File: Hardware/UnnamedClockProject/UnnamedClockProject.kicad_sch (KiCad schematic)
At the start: 7 parts, among them K101 DIR, K102 EN

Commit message: Bump upstream libs
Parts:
- added A101: Arduino_UNO_R3, Module:Arduino_UNO_R3, symbol MCU_Module:Arduino_UNO_R3
- added D103: FIX, LED_THT:LED_D5.0mm, symbol Device:LED
- added R103: 1k, symbol Device:R_Small
- added U102: ~, ac1ja:Ultimate GPS Breakout V3 Module, symbol ac1ja:Ultimate_GPS_Breakout_v3
- added U103: ~, ac1ja:DS3231, symbol ac1ja:DS3231_Breakout
- D101: value EN_LED -> EN
- D102: value DIR_LED -> DIR
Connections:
- net +5V: now also A101.5 (+5V), U102.8 (VIN), U103.1 (VIN)
- net GND: now also A101.29 (GND), A101.6 (GND), A101.7 (GND), D103.1 (K), U102.7 (GND), U103.2 (GND)
- new net: D103.2 (A), R103.2
- new net: R103.1, U102.4 (FIX)
- new net SCL: A101.14 (SCL/A5), U103.3 (SCL)
- new net SDA: A101.13 (SDA/A4), U103.4 (SDA)
- no-connect marks 1 -> 10

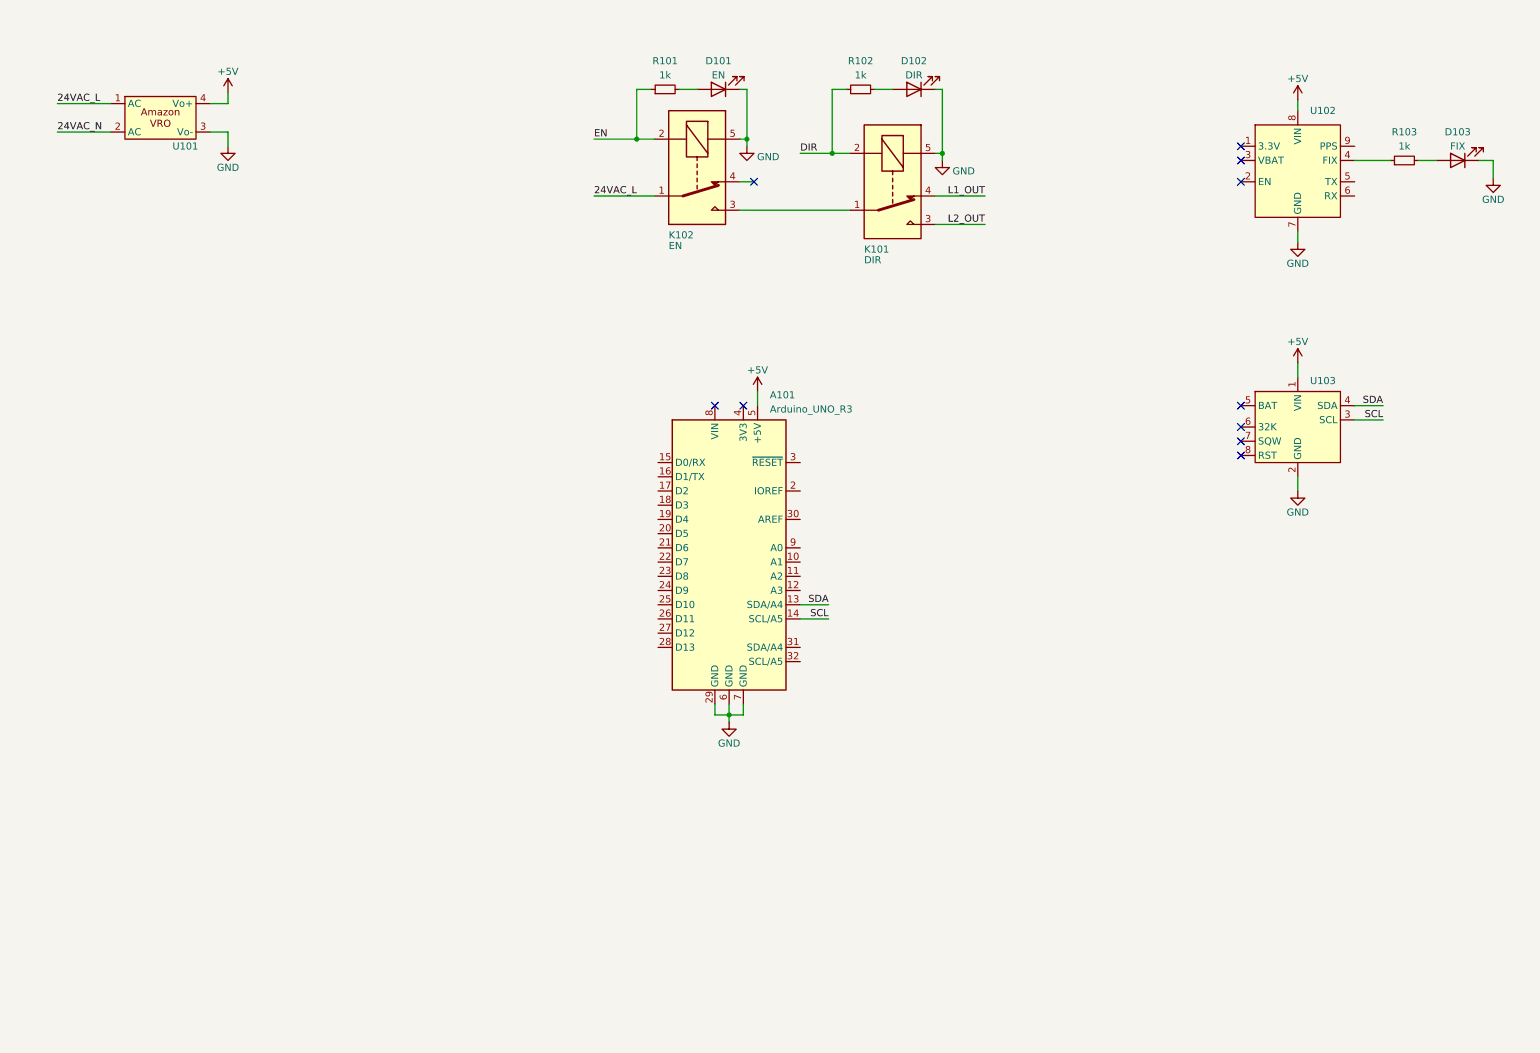
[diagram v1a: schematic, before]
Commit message: Add new design with solid state relays
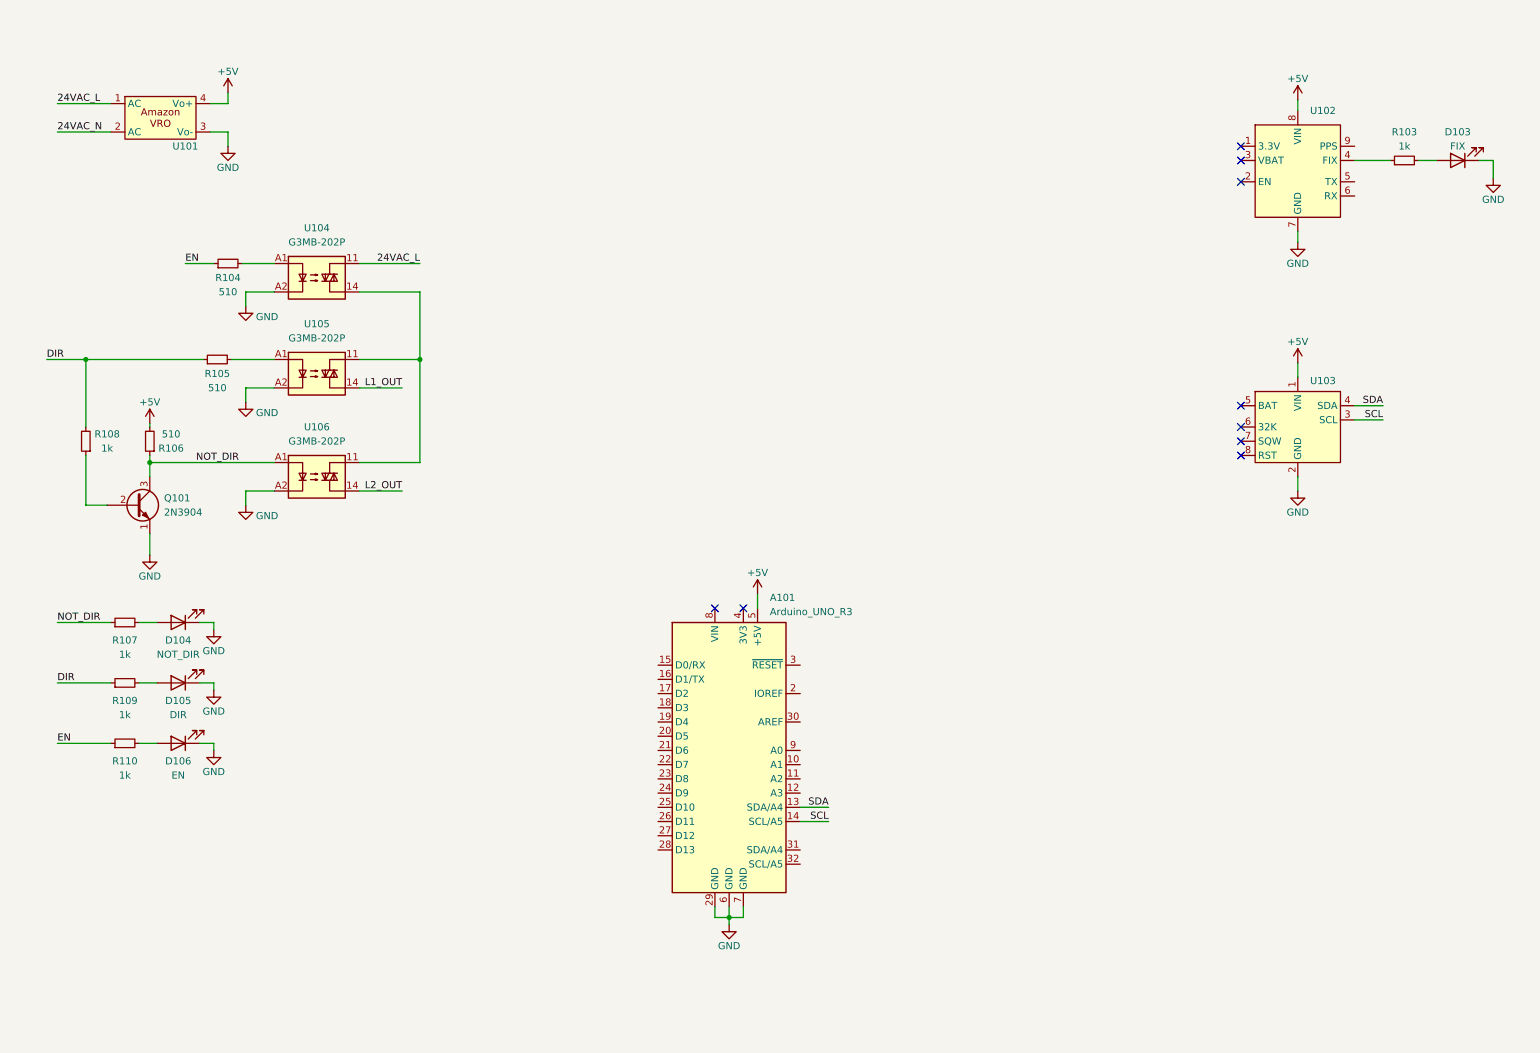
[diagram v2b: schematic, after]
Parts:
- removed D101: EN, LED_THT:LED_D5.0mm, symbol Device:LED
- removed D102: DIR, LED_THT:LED_D5.0mm, symbol Device:LED
- removed K101: DIR, Relay_THT:Relay_SPDT_SANYOU_SRD_Series_Form_C, symbol Relay:SANYOU_SRD_Form_C
- removed K102: EN, Relay_THT:Relay_SPDT_SANYOU_SRD_Series_Form_C, symbol Relay:SANYOU_SRD_Form_C
- removed R101, R102: 1k, symbol Device:R_Small
- added D104: NOT_DIR, LED_THT:LED_D5.0mm, symbol Device:LED
- added D105: DIR, LED_THT:LED_D5.0mm, symbol Device:LED
- added D106: EN, LED_THT:LED_D5.0mm, symbol Device:LED
- added Q101: 2N3904, Package_TO_SOT_THT:TO-92_Inline, symbol Transistor_BJT:2N3904
- added R104, R105, R106: 510, symbol Device:R_Small
- added R107, R108, R109, R110: 1k, symbol Device:R_Small
- added U104, U105, U106: G3MB-202P, symbol Relay_SolidState:34.81-8240
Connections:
- net +5V: now also R106.2
- net 24VAC_L: now also U104.11
- net DIR: now also R105.1, R108.2, R109.1
- net EN: now also R104.1, R110.1
- net GND: now also D104.1 (K), D105.1 (K), D106.1 (K), Q101.1 (E), U104.A2, U105.A2, U106.A2
- net L1_OUT: now also U105.14
- net L2_OUT: now also U106.14
- new net: U104.14, U105.11, U106.11
- new net: R104.2, U104.A1
- new net: D105.2 (A), R109.2
- new net: D106.2 (A), R110.2
- new net: D104.2 (A), R107.2
- new net: Q101.2 (B), R108.1
- new net: R105.2, U105.A1
- new net NOT_DIR: Q101.3 (C), R106.1, R107.1, U106.A1
- no-connect marks 10 -> 9
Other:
- moved on the sheet: A101

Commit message: Add footprints
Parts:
- U104, U105, U106: footprint (none) -> OptoDevice:Finder_34.81
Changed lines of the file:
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@@
       (effects (font (size 1.27 1.27)))
     )
-    (property "Footprint" "" (at 62.865 65.405 0)
+    (property "Footprint" "OptoDevice:Finder_34.81" (at 62.865 65.405 0)
       (effects (font (size 1.27 1.27) italic) (justify left) hide)
     )
@@
       (effects (font (size 1.27 1.27)))
     )
-    (property "Footprint" "" (at 62.865 82.55 0)
+    (property "Footprint" "OptoDevice:Finder_34.81" (at 62.865 82.55 0)
       (effects (font (size 1.27 1.27) italic) (justify left) hide)
     )
@@
       (effects (font (size 1.27 1.27)))
     )
-    (property "Footprint" "" (at 62.865 100.965 0)
+    (property "Footprint" "OptoDevice:Finder_34.81" (at 62.865 100.965 0)
       (effects (font (size 1.27 1.27) italic) (justify left) hide)
     )

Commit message: Add plugs
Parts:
- added J101: CLOCK_OUT, TerminalBlock_WAGO:TerminalBlock_WAGO_236-103_1x03_P5.00mm_45Degree, symbol Connector:Screw_Terminal_01x03
- added J102: POWER, TerminalBlock_WAGO:TerminalBlock_WAGO_236-103_1x03_P5.00mm_45Degree, symbol Connector:Screw_Terminal_01x03
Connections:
- net 24VAC_L: now also J102.1 (Pin_1)
- net 24VAC_N: now also J101.1 (Pin_1), J102.3 (Pin_3)
- net GND: now also J102.2 (Pin_2)
- net L1_OUT: now also J101.2 (Pin_2)
- net L2_OUT: now also J101.3 (Pin_3)
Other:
- moved on the sheet: D104, D105, D106, Q101, R104, R105, R106, R107, R108, R109, R110, U104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

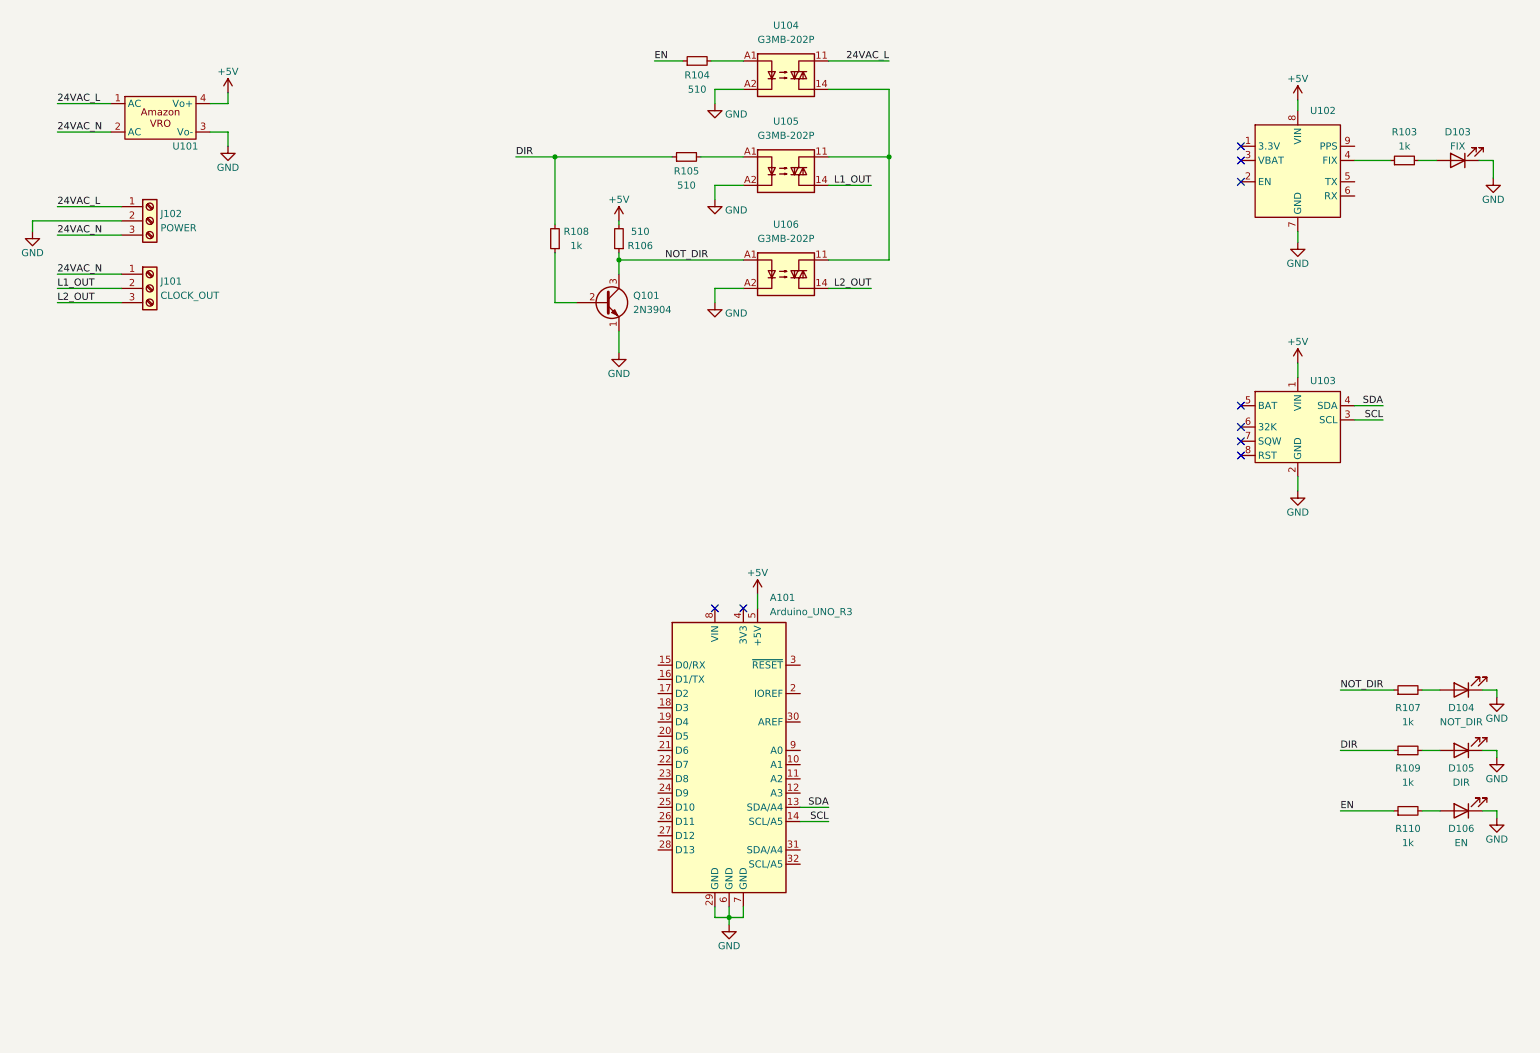
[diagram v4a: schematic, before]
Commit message: Tie into mcu
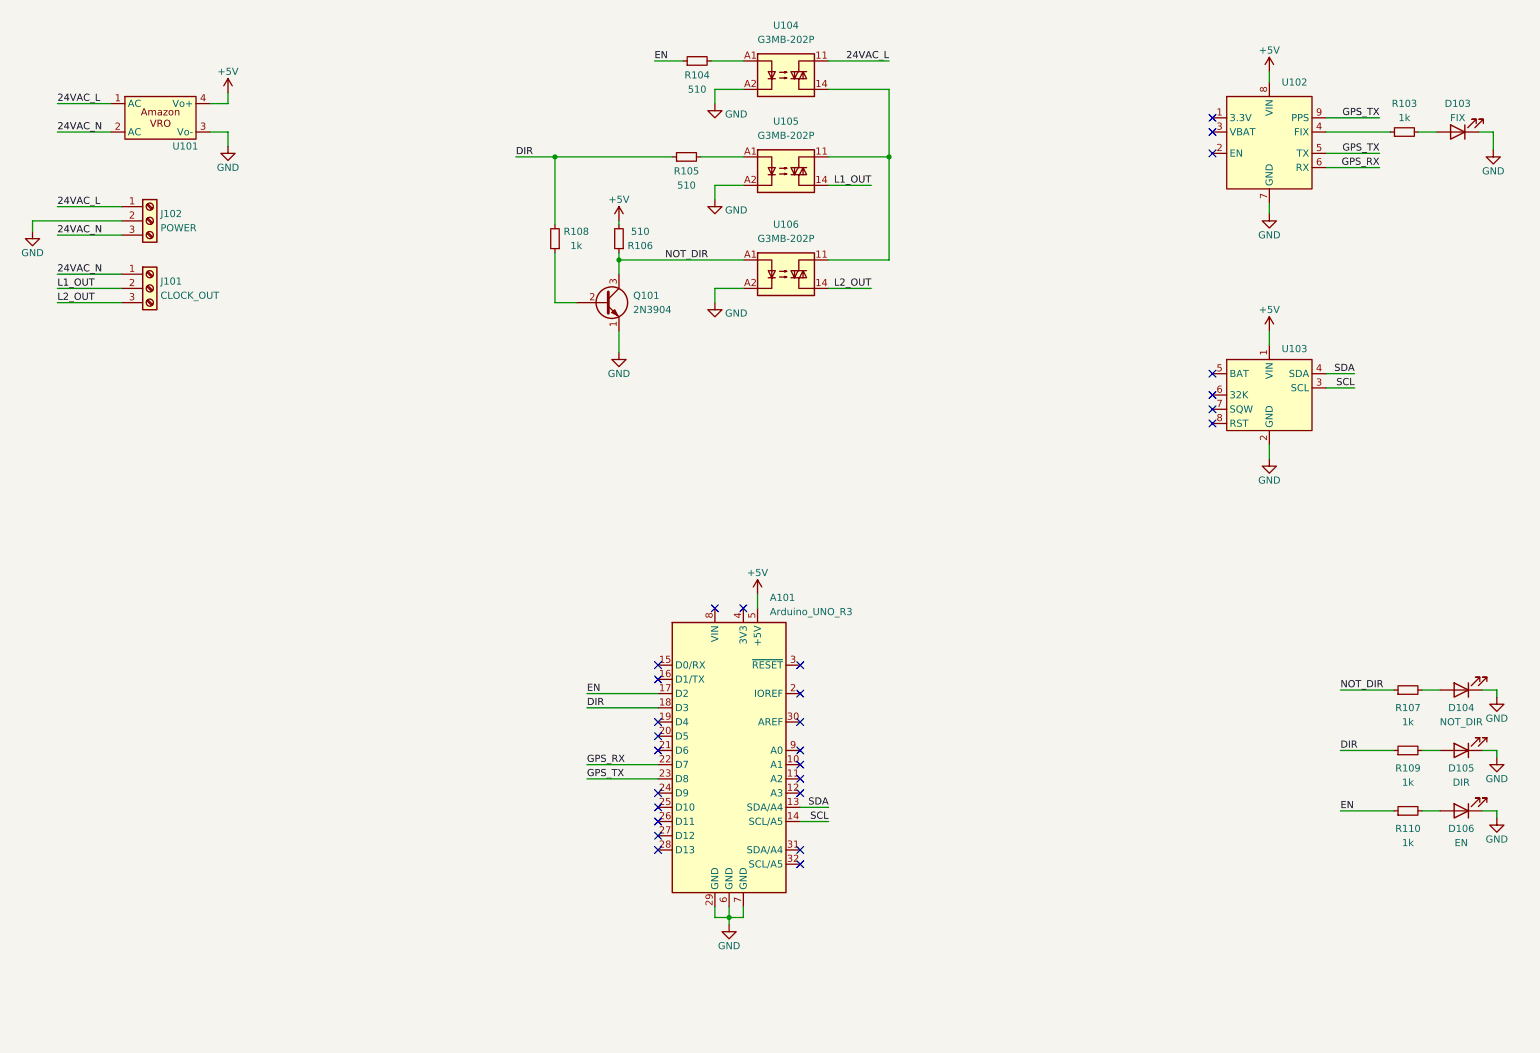
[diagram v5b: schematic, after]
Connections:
- net DIR: now also A101.18 (D3)
- net EN: now also A101.17 (D2)
- net GPS_TX: now reaches U102.5 (TX)
- net GPS_TX: now also A101.23 (D8), U102.9 (PPS)
- net GPS_RX: now reaches U102.6 (RX)
- net GPS_RX: now also A101.22 (D7)
- no-connect marks 9 -> 28
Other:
- moved on the sheet: D103, R103, U102, U103

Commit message: Add lcd from upstream
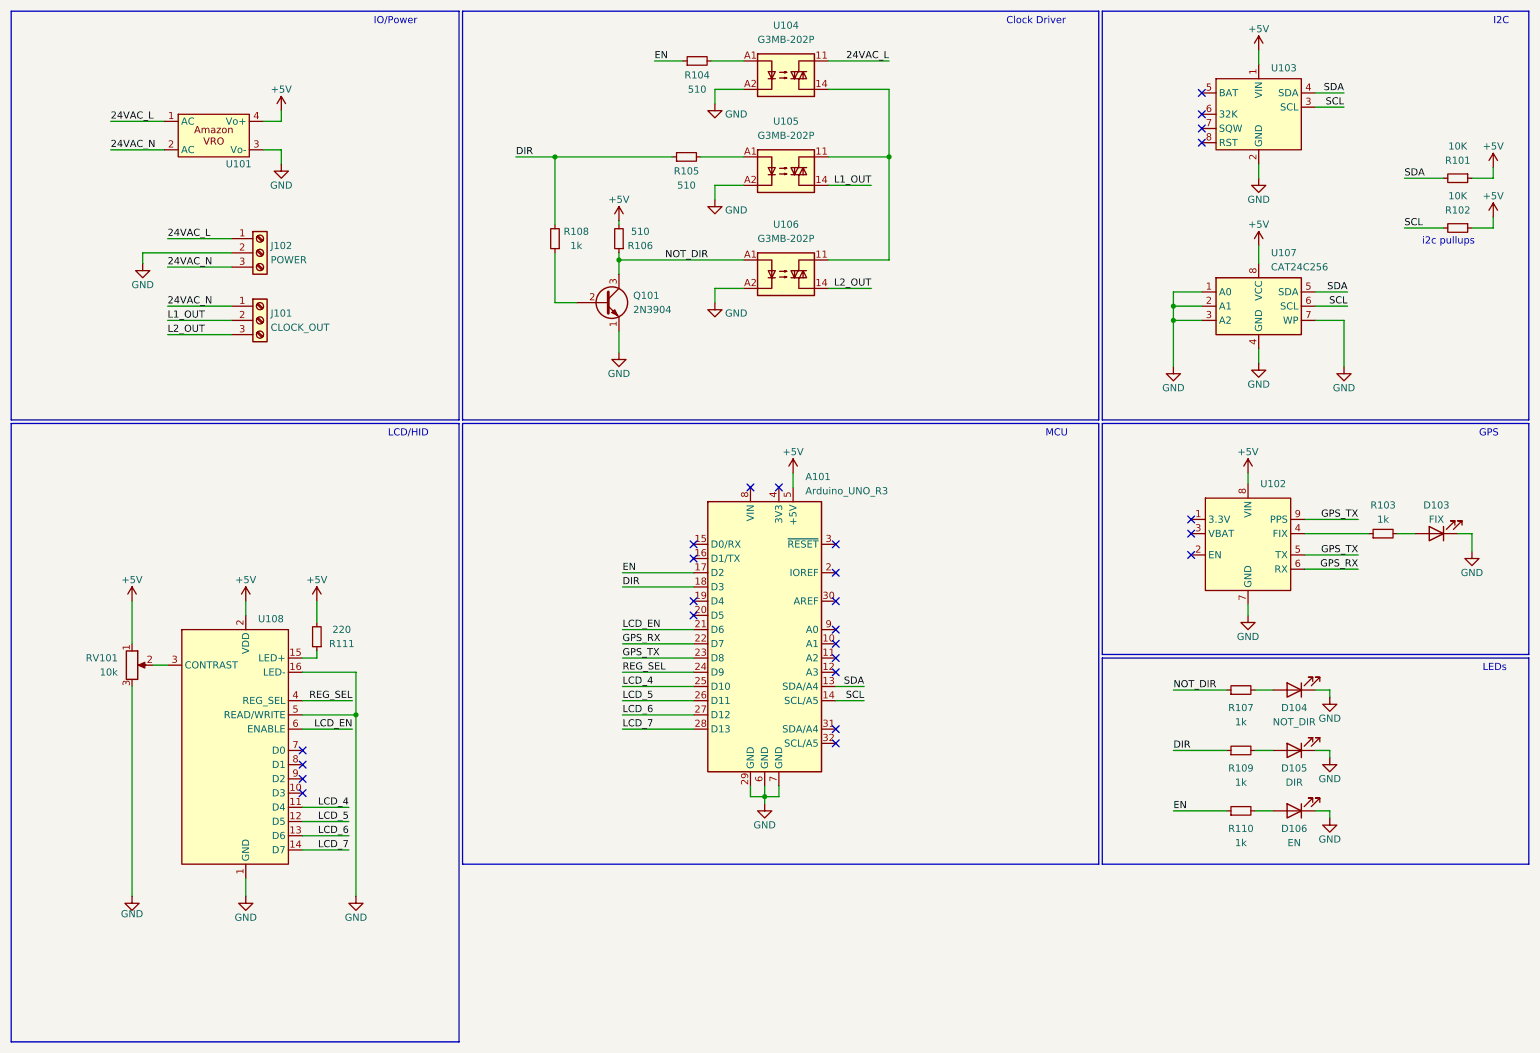
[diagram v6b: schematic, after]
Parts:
- added R101, R102: 10K, symbol Device:R_Small
- added R111: 220, symbol Device:R_Small
- added RV101: 10k, symbol Device:R_Potentiometer
- added U107: CAT24C256, Package_DIP:DIP-8_W7.62mm, symbol Memory_EEPROM:CAT24C256
- added U108: ~, ac1ja:2x16_LCD, symbol ac1ja:2x16_LCD
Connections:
- net +5V: now also R101.1, R102.1, R111.2, RV101.1, U107.8 (VCC), U108.2 (VDD)
- net GND: now also RV101.3, U107.1 (A0), U107.2 (A1), U107.3 (A2), U107.4 (GND), U107.7 (WP), U108.1 (GND), U108.16 (LED-), U108.5 (READ/WRITE)
- net SCL: now also R102.2, U107.6 (SCL)
- net SDA: now also R101.2, U107.5 (SDA)
- net LCD_EN: now reaches A101.21 (D6)
- net LCD_EN: now also U108.6 (ENABLE)
- net REG_SEL: now reaches A101.24 (D9)
- net REG_SEL: now also U108.4 (REG_SEL)
- net LCD_4: now reaches A101.25 (D10)
- net LCD_4: now also U108.11 (D4)
- net LCD_5: now reaches A101.26 (D11)
- net LCD_5: now also U108.12 (D5)
- net LCD_6: now reaches A101.27 (D12)
- net LCD_6: now also U108.13 (D6)
- net LCD_7: now reaches A101.28 (D13)
- net LCD_7: now also U108.14 (D7)
- new net: RV101.2, U108.3 (CONTRAST)
- new net: R111.1, U108.15 (LED+)
- no-connect marks 28 -> 26
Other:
- note added: "Clock Driver"
- note added: "GPS"
- note added: "I2C"
- note added: "IO/Power"
- note added: "LCD/HID"
- note added: "LEDs"
- note added: "MCU"
- note added: "i2c pullups"
- company: (none) -> Silvertech
- title: (none) -> Unnamed Clock Project
- moved on the sheet: A101, D103, D104, D105, D106, J101, J102, R103, R107, R109, R110, U101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
